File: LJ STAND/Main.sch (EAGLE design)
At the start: 213 parts, among them Q1 200mA/50V

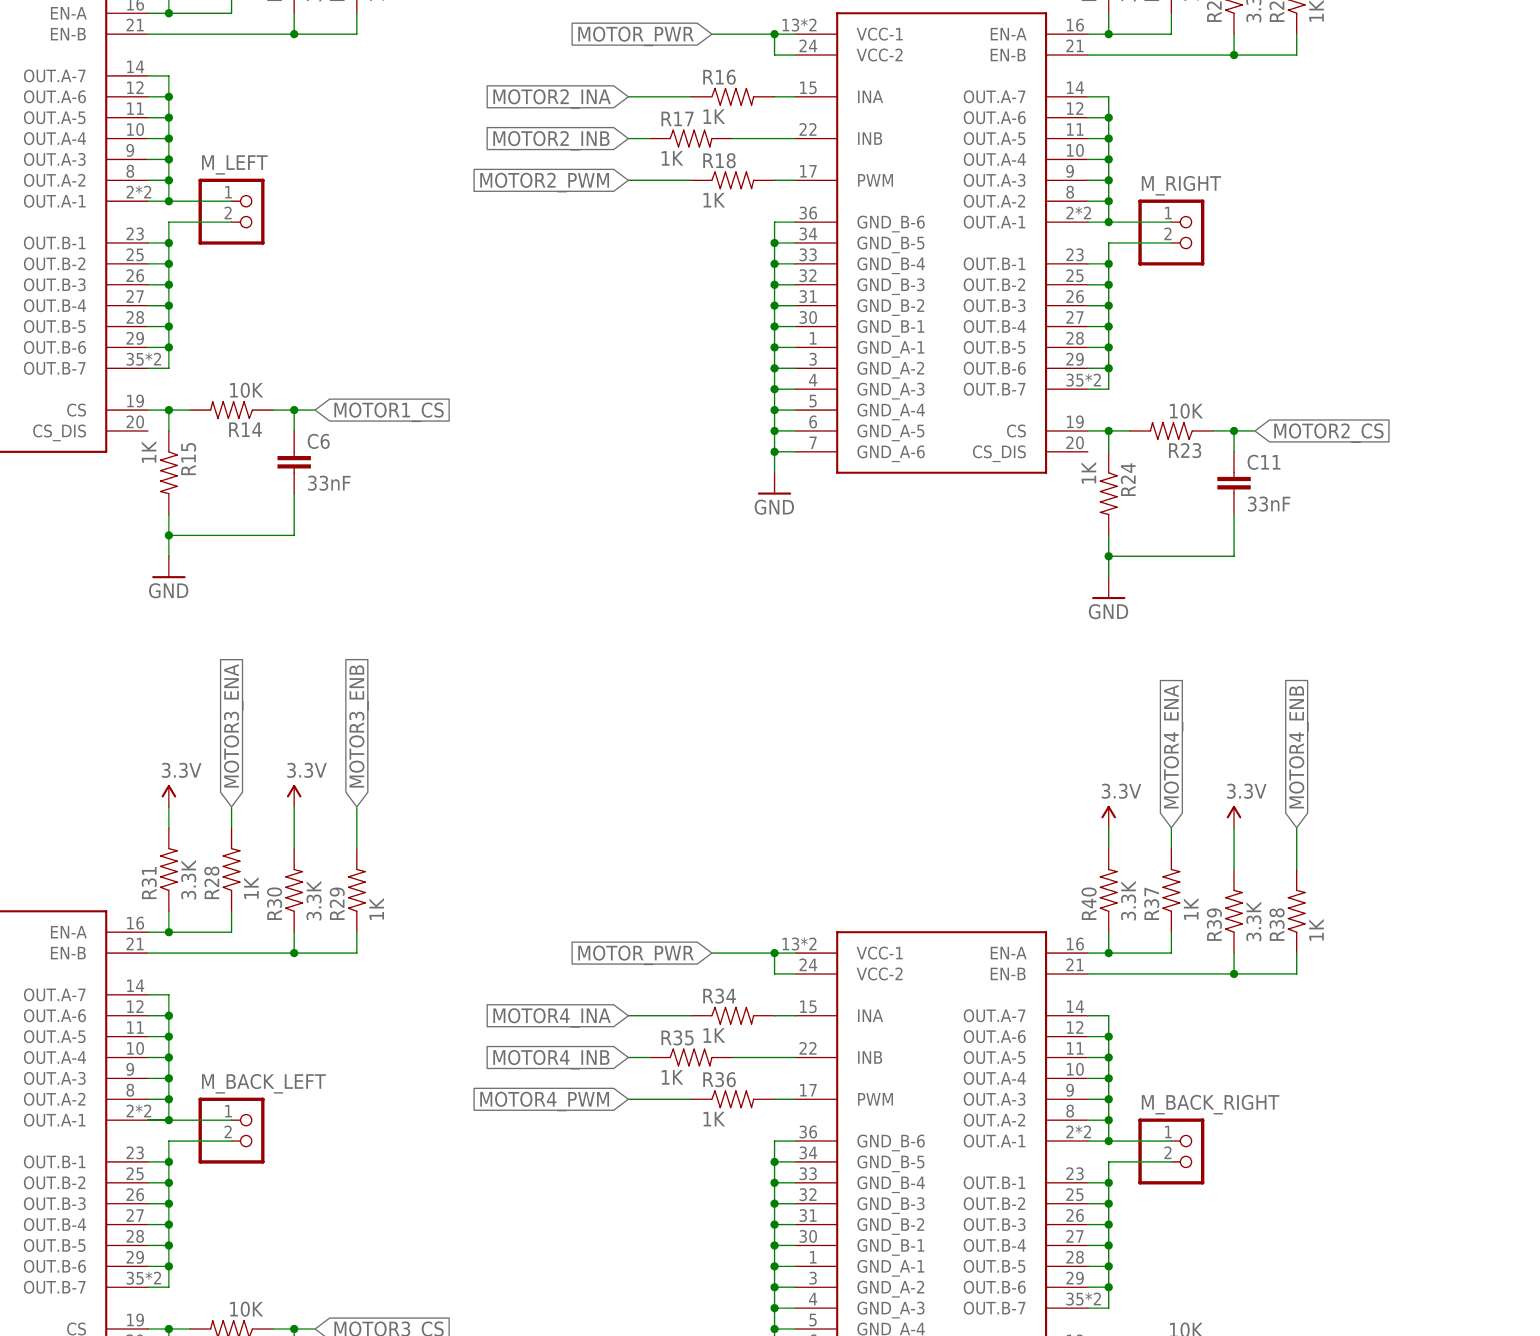
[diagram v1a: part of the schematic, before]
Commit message: Small fixes incl. grounding
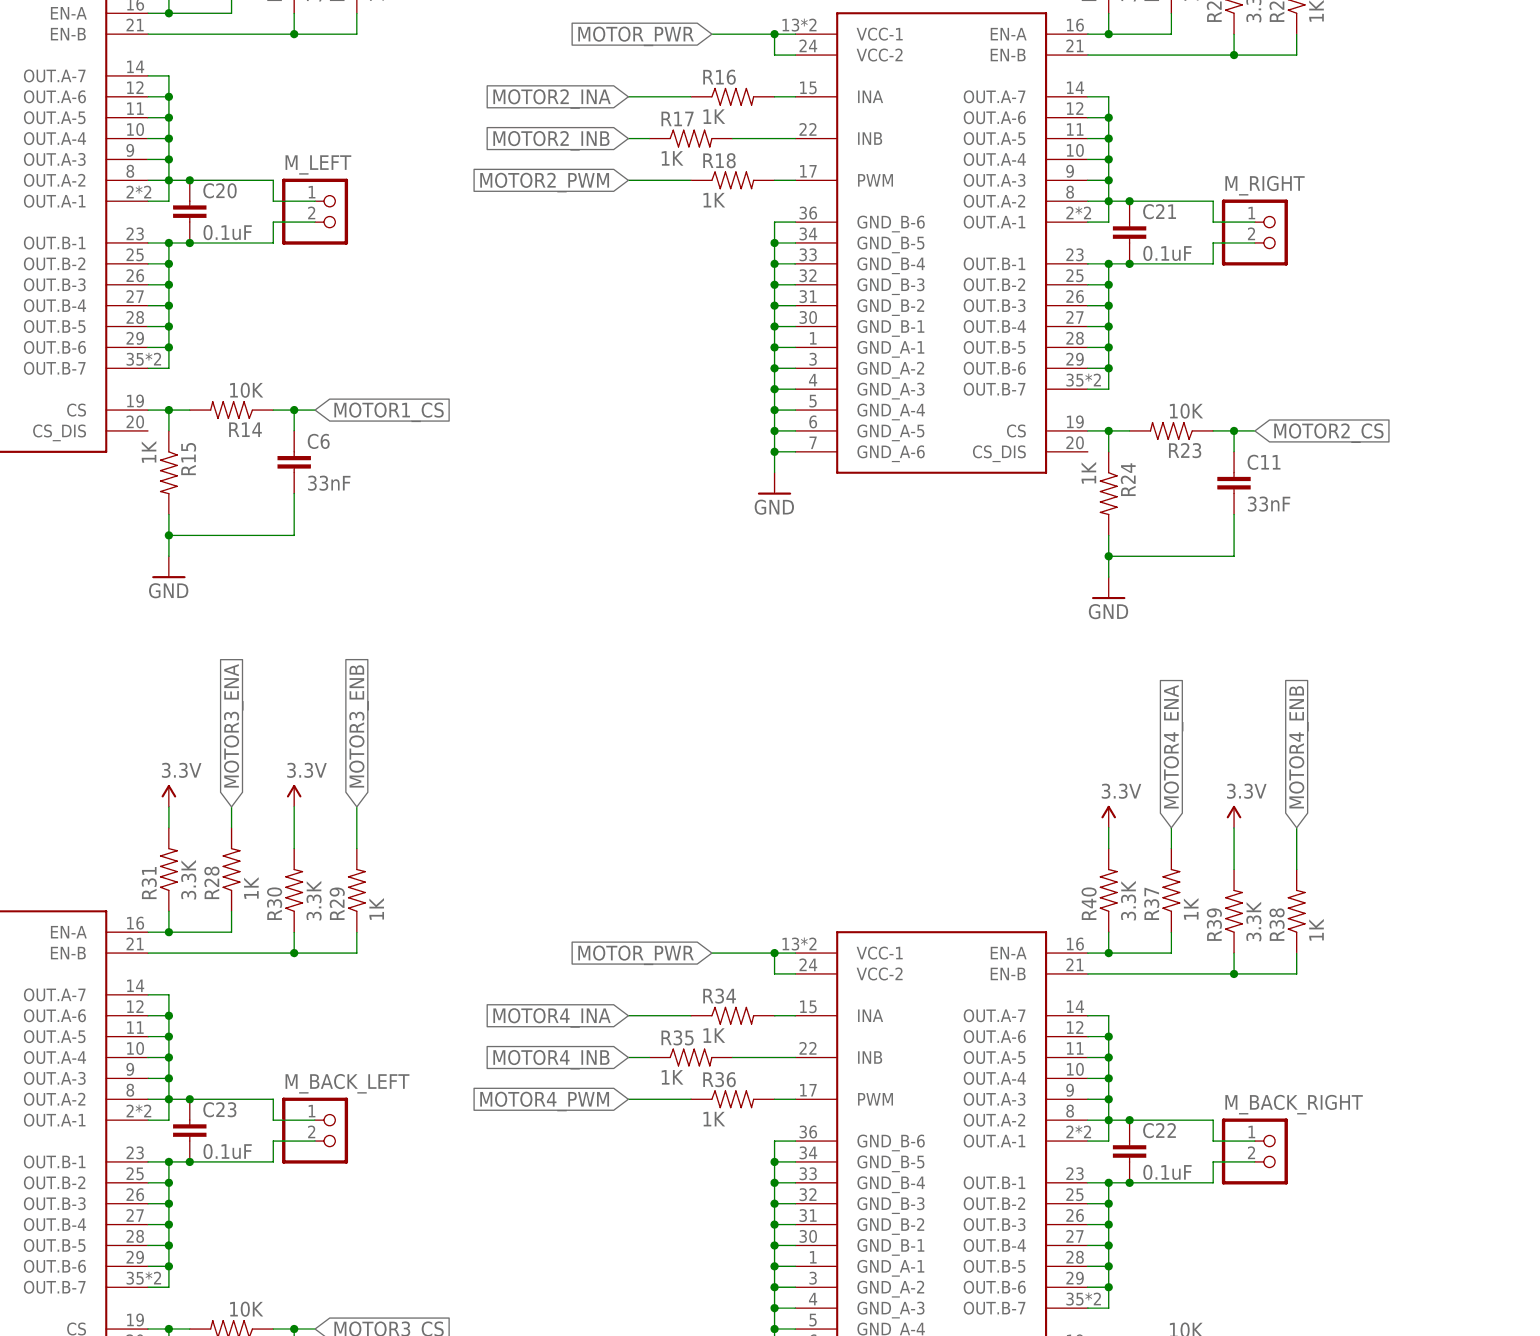
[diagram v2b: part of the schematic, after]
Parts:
- added C20, C21, C22, C23: 0.1uF, SparkFun-Capacitors:CAP0603-CAP
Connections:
- net MOTOR1_OUTA: now also C20.1
- net MOTOR1_OUTB: now also C20.2
- net MOTOR2_OUTA: now also C21.1
- net MOTOR2_OUTB: now also C21.2
- net MOTOR3_OUTA: now also C23.1
- net MOTOR3_OUTB: now also C23.2
- net MOTOR4_OUTA: now also C22.1
- net MOTOR4_OUTB: now also C22.2
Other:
- moved on the sheet: M_BACK_LEFT, M_BACK_RIGHT, M_LEFT, M_RIGHT
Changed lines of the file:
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@@
 <part name="GND101" library="SparkFun-Aesthetics" deviceset="GND" device=""/>
 <part name="GND102" library="SparkFun-Aesthetics" deviceset="GND" device=""/>
+<part name="C20" library="SparkFun-Capacitors" deviceset="CAP" device="0603-CAP" value="0.1uF"/>
+<part name="C21" library="SparkFun-Capacitors" deviceset="CAP" device="0603-CAP" value="0.1uF"/>
+<part name="C22" library="SparkFun-Capacitors" deviceset="CAP" device="0603-CAP" value="0.1uF"/>
+<part name="C23" library="SparkFun-Capacitors" deviceset="CAP" device="0603-CAP" value="0.1uF"/>
 </parts>
 <sheets>
@@
 <instance part="SUPPLY57" gate="G$1" x="-33.02" y="-347.98"/>
 <instance part="SUPPLY58" gate="G$1" x="-68.58" y="-347.98"/>
-<instance part="M_LEFT" gate="G$1" x="-33.02" y="-147.32"/>
-<instance part="M_RIGHT" gate="G$1" x="81.28" y="-149.86"/>
-<instance part="M_BACK_RIGHT" gate="G$1" x="81.28" y="-261.62"/>
-<instance part="M_BACK_LEFT" gate="G$1" x="-33.02" y="-259.08"/>
+<instance part="M_LEFT" gate="G$1" x="-22.86" y="-147.32"/>
+<instance part="M_RIGHT" gate="G$1" x="91.44" y="-149.86"/>
+<instance part="M_BACK_RIGHT" gate="G$1" x="91.44" y="-261.62"/>
+<instance part="M_BACK_LEFT" gate="G$1" x="-22.86" y="-259.08"/>
 <instance part="GND22" gate="1" x="246.38" y="-119.38"/>
 <instance part="GND23" gate="1" x="289.56" y="-119.38"/>
@@
 <instance part="GND101" gate="1" x="-132.08" y="-99.06"/>
 <instance part="GND102" gate="1" x="-248.92" y="-139.7"/>
+<instance part="C20" gate="G$1" x="-38.1" y="-149.86"/>
+<instance part="C21" gate="G$1" x="76.2" y="-152.4"/>
+<instance part="C22" gate="G$1" x="76.2" y="-264.16"/>
+<instance part="C23" gate="G$1" x="-38.1" y="-261.62"/>
 </instances>
 <busses>
@@
 <junction x="-40.64" y="-144.78"/>
 <junction x="-40.64" y="-142.24"/>
+<pinref part="C20" gate="G$1" pin="1"/>
+<wire x1="-40.64" y1="-144.78" x2="-38.1" y2="-144.78" width="0.1524" layer="91"/>
+<wire x1="-38.1" y1="-144.78" x2="-27.94" y2="-144.78" width="0.1524" layer="91"/>
+<wire x1="-27.94" y1="-144.78" x2="-27.94" y2="-147.32" width="0.1524" layer="91"/>
 <pinref part="M_LEFT" gate="G$1" pin="1"/>
-<wire x1="-40.64" y1="-147.32" x2="-33.02" y2="-147.32" width="0.1524" layer="91"/>
-<junction x="-40.64" y="-147.32"/>
+<wire x1="-27.94" y1="-147.32" x2="-22.86" y2="-147.32" width="0.1524" layer="91"/>
+<junction x="-38.1" y="-144.78"/>
 </segment>
 </net>
@@
 <pinref part="P1" gate="G$1" pin="OUT.B-2"/>
 <wire x1="-43.18" y1="-154.94" x2="-40.64" y2="-154.94" width="0.1524" layer="91"/>
-<junction x="-40.64" y="-152.4"/>
 <junction x="-40.64" y="-154.94"/>
 <junction x="-40.64" y="-157.48"/>
@@
 <junction x="-40.64" y="-162.56"/>
 <junction x="-40.64" y="-165.1"/>
+<pinref part="C20" gate="G$1" pin="2"/>
+<wire x1="-40.64" y1="-152.4" x2="-38.1" y2="-152.4" width="0.1524" layer="91"/>
 <pinref part="M_LEFT" gate="G$1" pin="2"/>
-<wire x1="-33.02" y1="-149.86" x2="-40.64" y2="-149.86" width="0.1524" layer="91"/>
-<wire x1="-40.64" y1="-149.86" x2="-40.64" y2="-152.4" width="0.1524" layer="91"/>
+<wire x1="-22.86" y1="-149.86" x2="-27.94" y2="-149.86" width="0.1524" layer="91"/>
+<wire x1="-27.94" y1="-149.86" x2="-27.94" y2="-152.4" width="0.1524" layer="91"/>
+<wire x1="-27.94" y1="-152.4" x2="-38.1" y2="-152.4" width="0.1524" layer="91"/>
+<junction x="-38.1" y="-152.4"/>
+<junction x="-40.64" y="-152.4"/>
 </segment>
 </net>
@@
 <junction x="73.66" y="-147.32"/>
 <junction x="73.66" y="-144.78"/>
+<pinref part="C21" gate="G$1" pin="1"/>
+<wire x1="73.66" y1="-147.32" x2="76.2" y2="-147.32" width="0.1524" layer="91"/>
 <pinref part="M_RIGHT" gate="G$1" pin="1"/>
-<wire x1="73.66" y1="-149.86" x2="81.28" y2="-149.86" width="0.1524" layer="91"/>
-<junction x="73.66" y="-149.86"/>
+<wire x1="86.36" y1="-147.32" x2="86.36" y2="-149.86" width="0.1524" layer="91"/>
+<wire x1="86.36" y1="-149.86" x2="91.44" y2="-149.86" width="0.1524" layer="91"/>
+<wire x1="86.36" y1="-147.32" x2="76.2" y2="-147.32" width="0.1524" layer="91"/>
+<junction x="76.2" y="-147.32"/>
 </segment>
 </net>
@@
 <pinref part="P2" gate="G$1" pin="OUT.B-2"/>
 <wire x1="71.12" y1="-157.48" x2="73.66" y2="-157.48" width="0.1524" layer="91"/>
-<junction x="73.66" y="-154.94"/>
 <junction x="73.66" y="-157.48"/>
 <junction x="73.66" y="-160.02"/>
@@
 <junction x="73.66" y="-165.1"/>
 <junction x="73.66" y="-167.64"/>
+<wire x1="73.66" y1="-154.94" x2="76.2" y2="-154.94" width="0.1524" layer="91"/>
+<wire x1="76.2" y1="-154.94" x2="86.36" y2="-154.94" width="0.1524" layer="91"/>
+<wire x1="86.36" y1="-154.94" x2="86.36" y2="-152.4" width="0.1524" layer="91"/>
 <pinref part="M_RIGHT" gate="G$1" pin="2"/>
-<wire x1="81.28" y1="-152.4" x2="73.66" y2="-152.4" width="0.1524" layer="91"/>
-<wire x1="73.66" y1="-152.4" x2="73.66" y2="-154.94" width="0.1524" layer="91"/>
+<wire x1="86.36" y1="-152.4" x2="91.44" y2="-152.4" width="0.1524" layer="91"/>
+<pinref part="C21" gate="G$1" pin="2"/>
+<junction x="76.2" y="-154.94"/>
+<junction x="73.66" y="-154.94"/>
 </segment>
 </net>
@@
 <segment>
 <pinref part="P3" gate="G$1" pin="OUT.A-1"/>
-<wire x1="-43.18" y1="-259.08" x2="-40.64" y2="-259.08" width="0.1524" layer="91"/>
 <wire x1="-40.64" y1="-259.08" x2="-40.64" y2="-256.54" width="0.1524" layer="91"/>
 <wire x1="-40.64" y1="-256.54" x2="-40.64" y2="-254" width="0.1524" layer="91"/>
@@
 <junction x="-40.64" y="-256.54"/>
 <junction x="-40.64" y="-254"/>
+<wire x1="-43.18" y1="-259.08" x2="-40.64" y2="-259.08" width="0.1524" layer="91"/>
+<pinref part="C23" gate="G$1" pin="1"/>
+<wire x1="-40.64" y1="-256.54" x2="-38.1" y2="-256.54" width="0.1524" layer="91"/>
+<wire x1="-38.1" y1="-256.54" x2="-27.94" y2="-256.54" width="0.1524" layer="91"/>
+<wire x1="-27.94" y1="-256.54" x2="-27.94" y2="-259.08" width="0.1524" layer="91"/>
+<junction x="-38.1" y="-256.54"/>
 <pinref part="M_BACK_LEFT" gate="G$1" pin="1"/>
-<wire x1="-43.18" y1="-259.08" x2="-40.64" y2="-259.08" width="0.1524" layer="91"/>
-<junction x="-40.64" y="-259.08"/>
-<wire x1="-40.64" y1="-259.08" x2="-33.02" y2="-259.08" width="0.1524" layer="91"/>
+<wire x1="-27.94" y1="-259.08" x2="-22.86" y2="-259.08" width="0.1524" layer="91"/>
 </segment>
 </net>
@@
 <junction x="-40.64" y="-274.32"/>
 <junction x="-40.64" y="-276.86"/>
+<wire x1="-27.94" y1="-261.62" x2="-27.94" y2="-264.16" width="0.1524" layer="91"/>
+<wire x1="-27.94" y1="-264.16" x2="-38.1" y2="-264.16" width="0.1524" layer="91"/>
+<junction x="-40.64" y="-264.16"/>
+<pinref part="C23" gate="G$1" pin="2"/>
+<junction x="-38.1" y="-264.16"/>
+<wire x1="-38.1" y1="-264.16" x2="-40.64" y2="-264.16" width="0.1524" layer="91"/>
 <pinref part="M_BACK_LEFT" gate="G$1" pin="2"/>
-<wire x1="-33.02" y1="-261.62" x2="-40.64" y2="-261.62" width="0.1524" layer="91"/>
-<wire x1="-40.64" y1="-261.62" x2="-40.64" y2="-264.16" width="0.1524" layer="91"/>
-<junction x="-40.64" y="-264.16"/>
+<wire x1="-27.94" y1="-261.62" x2="-22.86" y2="-261.62" width="0.1524" layer="91"/>
 </segment>
 </net>
@@
 <junction x="73.66" y="-259.08"/>
 <junction x="73.66" y="-256.54"/>
+<pinref part="C22" gate="G$1" pin="1"/>
+<wire x1="73.66" y1="-259.08" x2="76.2" y2="-259.08" width="0.1524" layer="91"/>
+<wire x1="76.2" y1="-259.08" x2="86.36" y2="-259.08" width="0.1524" layer="91"/>
+<wire x1="86.36" y1="-259.08" x2="86.36" y2="-261.62" width="0.1524" layer="91"/>
 <pinref part="M_BACK_RIGHT" gate="G$1" pin="1"/>
-<wire x1="81.28" y1="-261.62" x2="73.66" y2="-261.62" width="0.1524" layer="91"/>
-<junction x="73.66" y="-261.62"/>
+<wire x1="86.36" y1="-261.62" x2="91.44" y2="-261.62" width="0.1524" layer="91"/>
+<junction x="76.2" y="-259.08"/>
 </segment>
 </net>
@@
 <junction x="73.66" y="-276.86"/>
 <junction x="73.66" y="-279.4"/>
-<wire x1="73.66" y1="-266.7" x2="73.66" y2="-264.16" width="0.1524" layer="91"/>
 <pinref part="M_BACK_RIGHT" gate="G$1" pin="2"/>
-<wire x1="73.66" y1="-264.16" x2="81.28" y2="-264.16" width="0.1524" layer="91"/>
+<wire x1="91.44" y1="-264.16" x2="86.36" y2="-264.16" width="0.1524" layer="91"/>
+<wire x1="86.36" y1="-264.16" x2="86.36" y2="-266.7" width="0.1524" layer="91"/>
+<wire x1="73.66" y1="-266.7" x2="76.2" y2="-266.7" width="0.1524" layer="91"/>
 <junction x="73.66" y="-266.7"/>
-</segment>
-</net>
+<pinref part="C22" gate="G$1" pin="2"/>
+<junction x="76.2" y="-266.7"/>
+<wire x1="76.2" y1="-266.7" x2="86.36" y2="-266.7" width="0.1524" layer="91"/>
+</segment>
+</net>

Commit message: Final main + gerbers
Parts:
- C1: device SparkFun-Capacitors:1000UF-25V(PTH)KIT -> SparkFun-Capacitors:1000UF-25V(PTH)
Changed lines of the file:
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@@
 <part name="D1" library="PP_Passives" library_urn="urn:adsk.eagle:library:2306169" deviceset="DIODE" device="_D2PAK(TO-263AB)" package3d_urn="urn:adsk.eagle:package:2306289/2"/>
 <part name="VREG-5" library="V78-2000-switching-regulator" library_urn="urn:adsk.eagle:library:2307073" deviceset="V78-2000" device="" package3d_urn="urn:adsk.eagle:package:2307076/2"/>
-<part name="C1" library="SparkFun-Capacitors" deviceset="1000UF-25V(PTH)" device="KIT" value="1000uF"/>
+<part name="C1" library="SparkFun-Capacitors" deviceset="1000UF-25V(PTH)" device="" value="1000uF"/>
 <part name="GND2" library="SparkFun-Aesthetics" deviceset="GND" device=""/>
 <part name="MOTOR_FUSE" library="fuse-holder-3568" library_urn="urn:adsk.eagle:library:2307080" deviceset="3568-FUSEHOLDER" device="" package3d_urn="urn:adsk.eagle:package:2307083/2" value="30A"/>
